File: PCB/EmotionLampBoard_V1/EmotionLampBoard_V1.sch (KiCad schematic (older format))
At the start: 8 parts

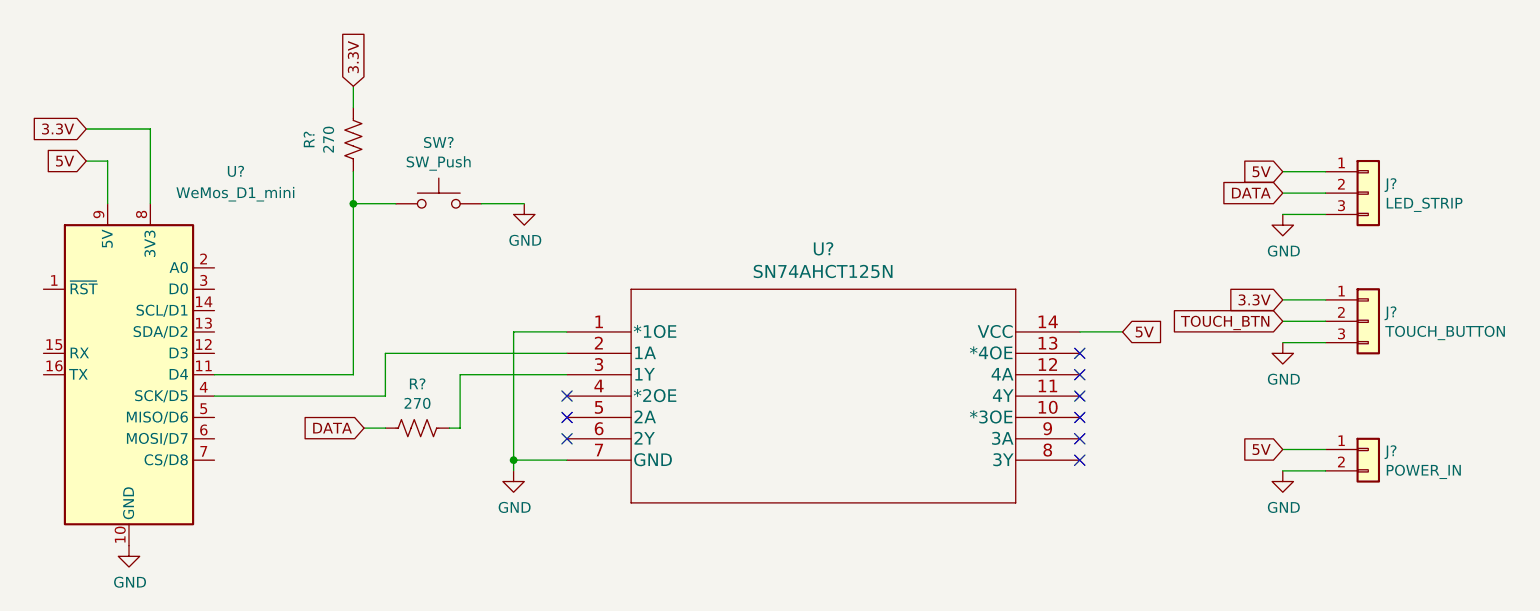
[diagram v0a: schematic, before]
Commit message: Fixed lamp buttons
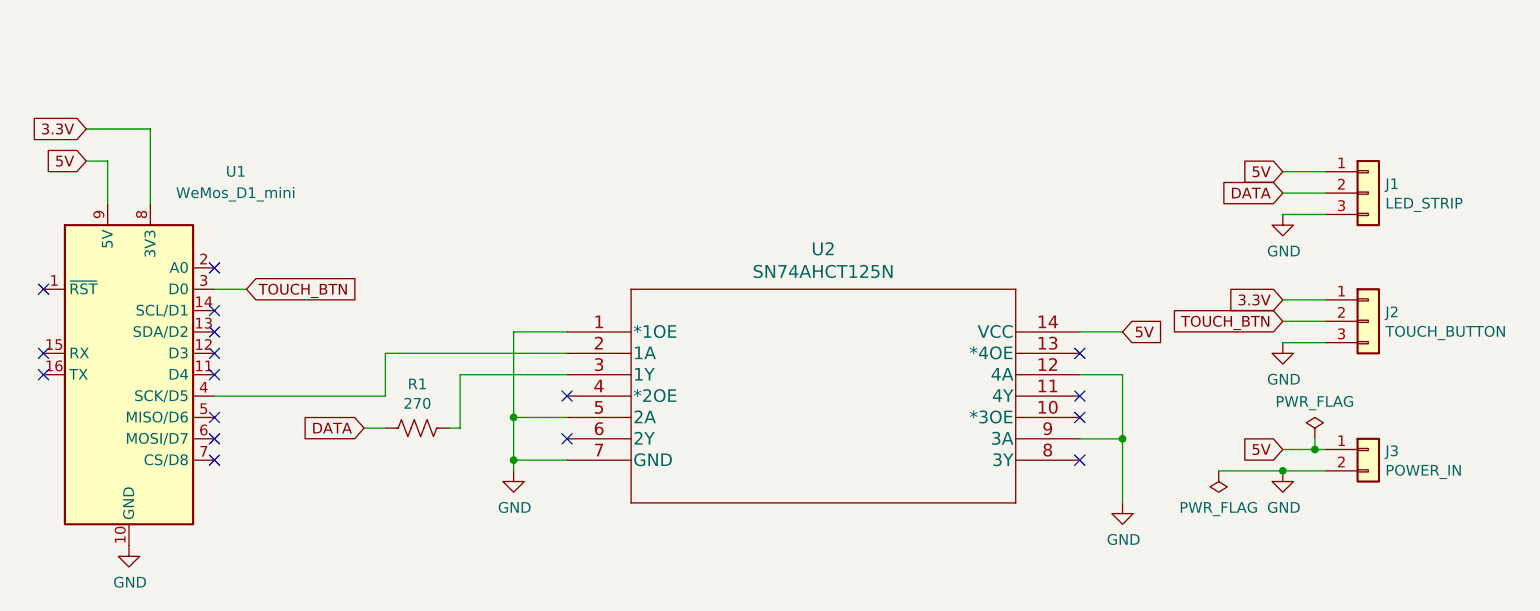
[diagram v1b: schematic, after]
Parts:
- removed R?: 270, symbol Device:R_US
- removed SW?: SW_Push, symbol Switch:SW_Push
- J1: renamed from J?; footprint (none) -> TB002-500-03BE:CUI_TB002-500-03BE
- J2: renamed from J?; footprint (none) -> Connector_PinHeader_2.54mm:PinHeader_1x03_P2.54mm_Vertical
- J3: renamed from J?; footprint (none) -> TB002-500-02BE:CUI_TB002-500-02BE
- R1: renamed from R?; footprint (none) -> Resistor_THT:R_Axial_DIN0207_L6.3mm_D2.5mm_P7.62mm_Horizontal
- U2: renamed from U?; footprint N14 -> 74AHCT125N:SN74AHCT125N
- gave numbers to parts that had none: 1
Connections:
- net GND: now also U2.12 (4A), U2.5 (2A), U2.9 (3A)
- net TOUCH_BTN: now also U1.3 (D0)
- no-connect marks 9 -> 17
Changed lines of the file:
@@
 $EndDescr
 $Comp
-L MCU_Module:WeMos_D1_mini U?
+L MCU_Module:WeMos_D1_mini U1
 U 1 1 61E710D5
 P 2150 2200
-F 0 "U?" H 2650 3150 50  0000 C CNN
+F 0 "U1" H 2650 3150 50  0000 C CNN
 F 1 "WeMos_D1_mini" H 2650 3050 50  0000 C CNN
 F 2 "Module:WEMOS_D1_mini_light" H 2150 1050 50  0001 C CNN
@@
 $EndComp
 $Comp
-L 74AHCT125N:SN74AHCT125N U?
+L 74AHCT125N:SN74AHCT125N U2
 U 1 1 61E71CAD
 P 4200 2000
-F 0 "U?" H 5400 2387 60  0000 C CNN
+F 0 "U2" H 5400 2387 60  0000 C CNN
 F 1 "SN74AHCT125N" H 5400 2281 60  0000 C CNN
-F 2 "N14" H 5400 2240 60  0001 C CNN
+F 2 "74AHCT125N:SN74AHCT125N" H 5400 2240 60  0001 C CNN
 F 3 "" H 4200 2000 60  0000 C CNN
 	1    4200 2000
@@
 	6800 2000 6600 2000
 $Comp
-L power:GND #PWR?
+L power:GND #PWR0101
 U 1 1 61E72DC7
 P 3950 2650
-F 0 "#PWR?" H 3950 2400 50  0001 C CNN
+F 0 "#PWR0101" H 3950 2400 50  0001 C CNN
 F 1 "GND" H 3955 2477 50  0000 C CNN
 F 2 "" H 3950 2650 50  0001 C CNN
@@
 	3350 2100 4200 2100
 Wire Wire Line
-	3950 2600 3950 2000
+	3950 2600 3950 2400
 Wire Wire Line
 	3950 2000 4200 2000
@@
 	2250 1050 2250 1400
 $Comp
-L power:GND #PWR?
+L power:GND #PWR0102
 U 1 1 61E74131
 P 2150 3000
-F 0 "#PWR?" H 2150 2750 50  0001 C CNN
+F 0 "#PWR0102" H 2150 2750 50  0001 C CNN
 F 1 "GND" H 2155 2827 50  0000 C CNN
 F 2 "" H 2150 3000 50  0001 C CNN
@@
 $EndComp
 $Comp
-L Connector_Generic:Conn_01x03 J?
+L Connector_Generic:Conn_01x03 J1
 U 1 1 61E758B9
 P 7950 1350
-F 0 "J?" H 8030 1392 50  0000 L CNN
+F 0 "J1" H 8030 1392 50  0000 L CNN
 F 1 "LED_STRIP" H 8030 1301 50  0000 L CNN
-F 2 "" H 7950 1350 50  0001 C CNN
+F 2 "TB002-500-03BE:CUI_TB002-500-03BE" H 7950 1350 50  0001 C CNN
 F 3 "~" H 7950 1350 50  0001 C CNN
 	1    7950 1350
@@
 Text GLabel 7550 1250 0    50   Input ~ 0
 5V
-Text GLabel 7550 1350 0    50   Input ~ 0
-DATA
-$Comp
-L power:GND #PWR?
+$Comp
+L power:GND #PWR0103
 U 1 1 61E76A0B
 P 7550 1450
-F 0 "#PWR?" H 7550 1200 50  0001 C CNN
+F 0 "#PWR0103" H 7550 1200 50  0001 C CNN
 F 1 "GND" H 7555 1277 50  0000 C CNN
 F 2 "" H 7550 1450 50  0001 C CNN
@@
 Wire Wire Line
 	7750 1450 7550 1450
-Text GLabel 3250 2450 0    50   Input ~ 0
-DATA
-$Comp
-L Device:R_US R?
+$Comp
+L Device:R_US R1
 U 1 1 61E77868
 P 3500 2450
-F 0 "R?" V 3295 2450 50  0000 C CNN
+F 0 "R1" V 3295 2450 50  0000 C CNN
 F 1 "270" V 3386 2450 50  0000 C CNN
-F 2 "" V 3540 2440 50  0001 C CNN
+F 2 "Resistor_THT:R_Axial_DIN0207_L6.3mm_D2.5mm_P7.62mm_Horizontal" V 3540 2440 50  0001 C CNN
 F 3 "~" H 3500 2450 50  0001 C CNN
 	1    3500 2450
@@
 Wire Wire Line
 	3700 2450 3650 2450
-NoConn ~ 4200 2400
 NoConn ~ 4200 2500
-NoConn ~ 6600 2200
 NoConn ~ 6600 2300
-NoConn ~ 6600 2500
 NoConn ~ 6600 2600
 $Comp
-L Connector_Generic:Conn_01x03 J?
+L Connector_Generic:Conn_01x03 J2
 U 1 1 61E793FA
 P 7950 1950
-F 0 "J?" H 8030 1992 50  0000 L CNN
+F 0 "J2" H 8030 1992 50  0000 L CNN
 F 1 "TOUCH_BUTTON" H 8030 1901 50  0000 L CNN
-F 2 "" H 7950 1950 50  0001 C CNN
+F 2 "Connector_PinHeader_2.54mm:PinHeader_1x03_P2.54mm_Vertical" H 7950 1950 50  0001 C CNN
 F 3 "~" H 7950 1950 50  0001 C CNN
 	1    7950 1950
@@
 TOUCH_BTN
 $Comp
-L power:GND #PWR?
+L power:GND #PWR0104
 U 1 1 61E79DF6
 P 7550 2050
-F 0 "#PWR?" H 7550 1800 50  0001 C CNN
+F 0 "#PWR0104" H 7550 1800 50  0001 C CNN
 F 1 "GND" H 7555 1877 50  0000 C CNN
 F 2 "" H 7550 2050 50  0001 C CNN
@@
 	7750 2050 7550 2050
 $Comp
-L Connector_Generic:Conn_01x02 J?
+L Connector_Generic:Conn_01x02 J3
 U 1 1 61E7C24C
 P 7950 2550
-F 0 "J?" H 8030 2542 50  0000 L CNN
+F 0 "J3" H 8030 2542 50  0000 L CNN
 F 1 "POWER_IN" H 8030 2451 50  0000 L CNN
-F 2 "" H 7950 2550 50  0001 C CNN
+F 2 "TB002-500-02BE:CUI_TB002-500-02BE" H 7950 2550 50  0001 C CNN
 F 3 "~" H 7950 2550 50  0001 C CNN
 	1    7950 2550
@@
 $EndComp
 $Comp
-L power:GND #PWR?
+L power:GND #PWR0105
 U 1 1 61E7CBA8
 P 7550 2650
-F 0 "#PWR?" H 7550 2400 50  0001 C CNN
+F 0 "#PWR0105" H 7550 2400 50  0001 C CNN
 F 1 "GND" H 7555 2477 50  0000 C CNN
 F 2 "" H 7550 2650 50  0001 C CNN
@@
 5V
 Wire Wire Line
-	7750 2550 7550 2550
+	7750 2550 7700 2550
 NoConn ~ 4200 2300
 NoConn ~ 6600 2400
 NoConn ~ 6600 2100
-$Comp
-L Switch:SW_Push SW?
-U 1 1 61E7DC50
-P 3600 1400
-F 0 "SW?" H 3600 1685 50  0000 C CNN
-F 1 "SW_Push" H 3600 1594 50  0000 C CNN
-F 2 "" H 3600 1600 50  0001 C CNN
-F 3 "~" H 3600 1600 50  0001 C CNN
-	1    3600 1400
-	1    0    0    -1
-$EndComp
-Wire Wire Line
-	3400 1400 3200 1400
-Wire Wire Line
-	3200 1400 3200 2200
-Wire Wire Line
-	3200 2200 2550 2200
-$Comp
-L power:GND #PWR?
-U 1 1 61E807C5
-P 4000 1400
-F 0 "#PWR?" H 4000 1150 50  0001 C CNN
-F 1 "GND" H 4005 1227 50  0000 C CNN
-F 2 "" H 4000 1400 50  0001 C CNN
-F 3 "" H 4000 1400 50  0001 C CNN
-	1    4000 1400
-	1    0    0    -1
-$EndComp
-Wire Wire Line
-	4000 1400 3800 1400
-$Comp
-L Device:R_US R?
-U 1 1 61E81E7E
-P 3200 1100
-F 0 "R?" V 2995 1100 50  0000 C CNN
-F 1 "270" V 3086 1100 50  0000 C CNN
-F 2 "" V 3240 1090 50  0001 C CNN
-F 3 "~" H 3200 1100 50  0001 C CNN
-	1    3200 1100
-	1    0    0    -1
-$EndComp
-Text GLabel 3200 850  1    50   Input ~ 0
-3.3V
-Wire Wire Line
-	3200 850  3200 950
-Wire Wire Line
-	3200 1250 3200 1400
-Connection ~ 3200 1400
+Wire Wire Line
+	4200 2400 3950 2400
+Connection ~ 3950 2400
+Wire Wire Line
+	3950 2400 3950 2000
+Wire Wire Line
+	6600 2200 6800 2200
+Wire Wire Line
+	6800 2200 6800 2500
+Wire Wire Line
+	6800 2500 6600 2500
+$Comp
+L power:GND #PWR0106
+U 1 1 61ED28ED
+P 6800 2800
+F 0 "#PWR0106" H 6800 2550 50  0001 C CNN
+F 1 "GND" H 6805 2627 50  0000 C CNN
+F 2 "" H 6800 2800 50  0001 C CNN
+F 3 "" H 6800 2800 50  0001 C CNN
+	1    6800 2800
+	1    0    0    -1
+$EndComp
+Wire Wire Line
+	6800 2500 6800 2800
+Connection ~ 6800 2500
+Text GLabel 2700 1800 2    50   Input ~ 0
+TOUCH_BTN
+Wire Wire Line
+	2700 1800 2550 1800
+NoConn ~ 1750 1800
+NoConn ~ 1750 2100
+NoConn ~ 1750 2200
+NoConn ~ 2550 1700
+NoConn ~ 2550 1900
+NoConn ~ 2550 2000
+NoConn ~ 2550 2100
+NoConn ~ 2550 2200
+NoConn ~ 2550 2400
+NoConn ~ 2550 2500
+NoConn ~ 2550 2600
+$Comp
+L power:PWR_FLAG #FLG0101
+U 1 1 61ED7CD1
+P 7700 2500
+F 0 "#FLG0101" H 7700 2575 50  0001 C CNN
+F 1 "PWR_FLAG" H 7700 2673 50  0000 C CNN
+F 2 "" H 7700 2500 50  0001 C CNN
+F 3 "~" H 7700 2500 50  0001 C CNN
+	1    7700 2500
+	1    0    0    -1
+$EndComp
+Wire Wire Line
+	7700 2500 7700 2550
+Connection ~ 7700 2550
+Wire Wire Line
+	7700 2550 7550 2550
+$Comp
+L power:PWR_FLAG #FLG0102
+U 1 1 61ED996C
+P 7250 2650
+F 0 "#FLG0102" H 7250 2725 50  0001 C CNN
+F 1 "PWR_FLAG" H 7250 2823 50  0000 C CNN
+F 2 "" H 7250 2650 50  0001 C CNN
+F 3 "~" H 7250 2650 50  0001 C CNN
+	1    7250 2650
+	-1   0    0    1
+$EndComp
+Wire Wire Line
+	7550 2650 7250 2650
+Connection ~ 7550 2650
+Text GLabel 7550 1350 0    50   Input ~ 0
+DATA
+Text GLabel 3250 2450 0    50   Input ~ 0
+DATA
 $EndSCHEMATC
